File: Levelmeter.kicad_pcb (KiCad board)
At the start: 4 copper layers, 90 x 70 mm, 178 parts, among them J1 JST_PH_2.0mm_1x02, J10 Header_50mil_1x05, J11 Header_50mil_1x05, J2 USB_C, J3 Header_50mil_2x07, J4 JST_PH_2.0mm_1x03, J5 Header_100mil_1x06, J6 Header_100mil_1x06, J7 Header_100mil_1x06, J8 Header_50mil_1x03, J9 Header_50mil_1x05, Q1 DMG2305UX-13, Q2 DMG2305UX-13, Q3 FS8205A, Q4 AO3400A, Q5 AO3400A, SW1 PEC11R-4215F-S0024, SW2 PEC11R-4215F-S0024, U1 LP5907MFX-3.3/NOPB, U10 BL24C256A-SFRC, U11 BME280, U12 SN74HC14PWR, U13 LM35, U14 AD9833BRMZ-REEL7, U15 ADS131M04IPWR, U16 AD826, U2 DW01A, U3 LP5907MFX-3.3/NOPB, U4 TP4056, U5 HX4002-MFC, U6 LM27761DSGR, U7 STM32G0B1RET6, U8 RN4871-I/RM128, U9 SN74AHCT244DBR, Y1 Q13FC1350000400, Y2 X50328MSB2GI

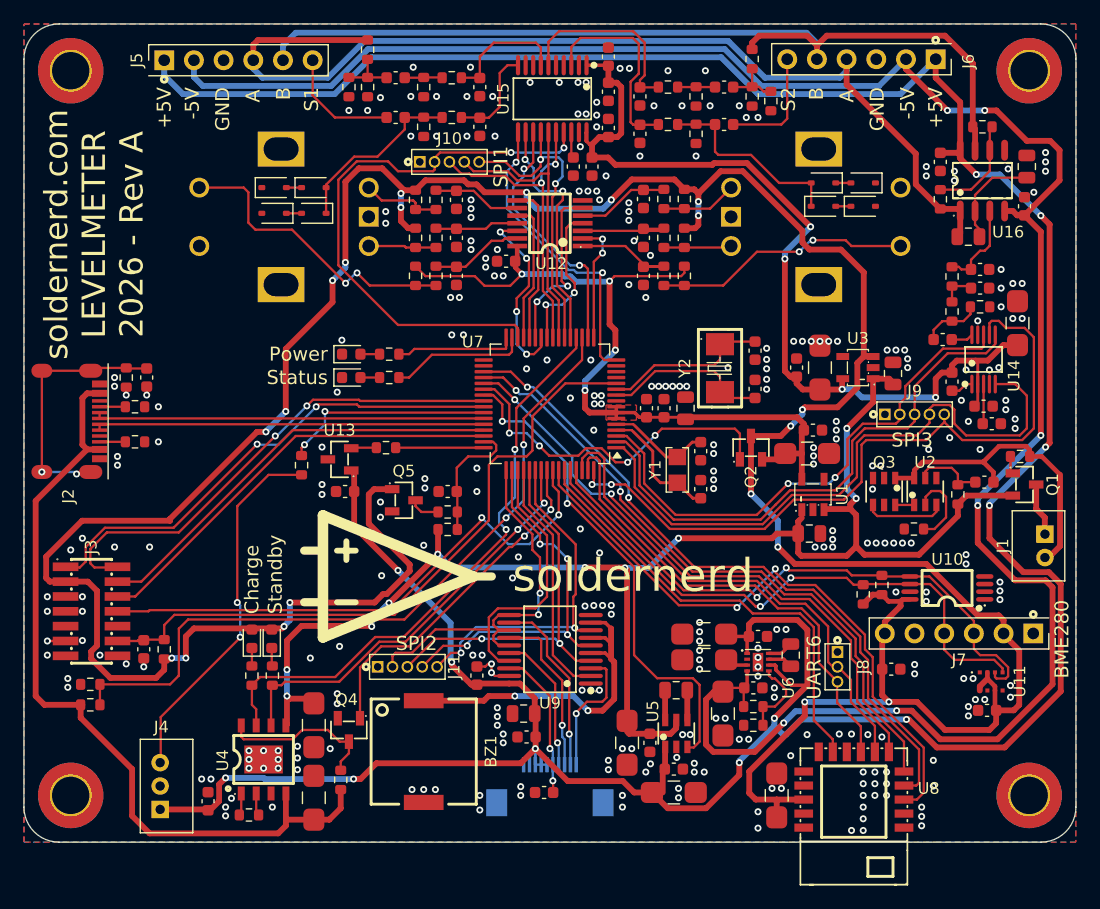
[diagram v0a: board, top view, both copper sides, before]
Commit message: Levelmeter sensor pinout changed. Font changed to bold
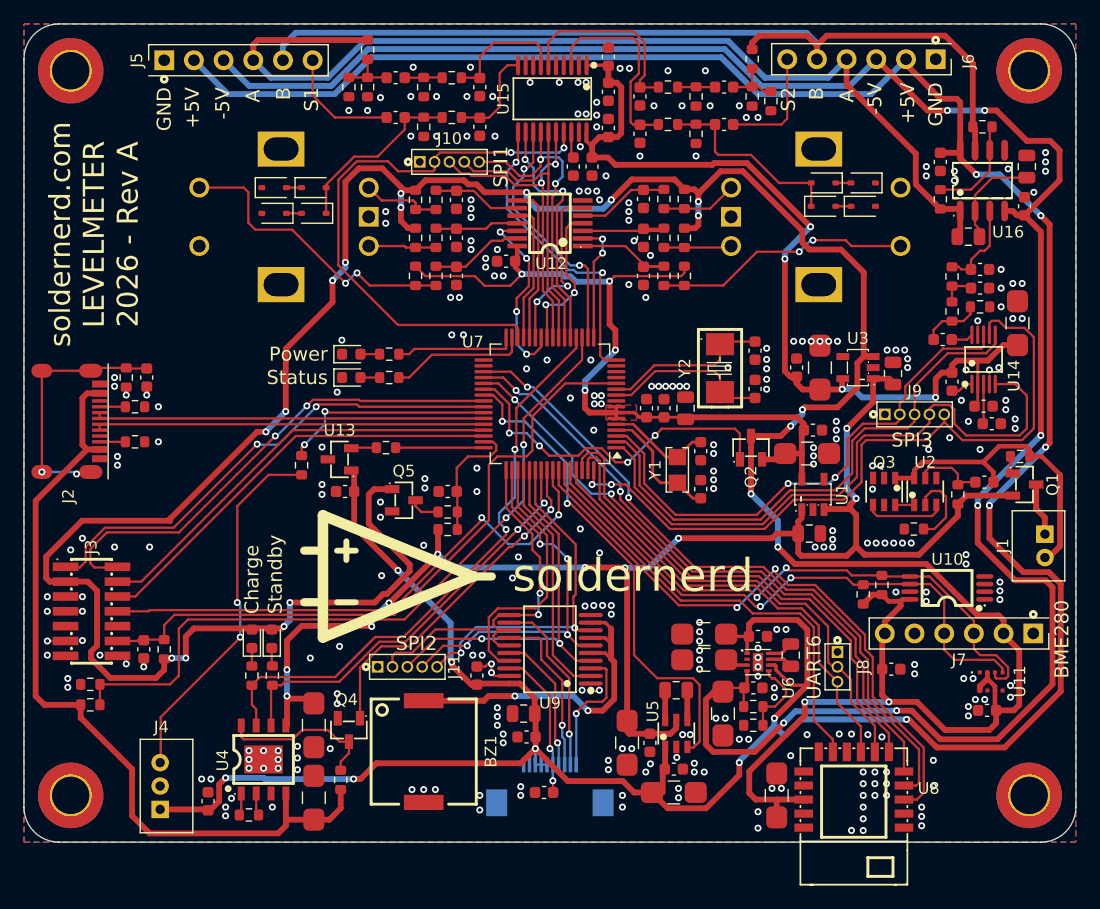
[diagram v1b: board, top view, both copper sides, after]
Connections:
- J5 pad 1: 5V0 -> GND
- J5 pad 2: -4V5 -> 5V0
- J5 pad 3: GND -> -4V5
- J6 pad 1: 5V0 -> GND
- J6 pad 2: -4V5 -> 5V0
- J6 pad 3: GND -> -4V5
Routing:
- net 5V0: track 292.1 -> 288.0 mm
- net -4V5: track 184.0 -> 180.0 mm
- net ExciterA: track 87.2 -> 86.0 mm

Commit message: Pinout description added, STM configuration added, netlist exported
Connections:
- net ~{CHARGE_EN} renamed CHARGE_EN
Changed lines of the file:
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@@
 			(size 1.25 0.7)
 			(layers "F.Cu" "F.Mask" "F.Paste")
-			(net "~{CHARGE_EN}")
+			(net "CHARGE_EN")
 			(pinfunction "G_1")
 			(pintype "unspecified")
@@
 			(layers "F.Cu" "F.Mask" "F.Paste")
 			(roundrect_rratio 0.25)
-			(net "~{CHARGE_EN}")
+			(net "CHARGE_EN")
 			(pinfunction "PD6_56")
 			(pintype "bidirectional")
@@
 	)
 	(segment
-		(start 94.75 68.175)
-		(end 94.75 70.375983)
-		(width 0.2)
-		(layer "F.Cu")
-		(net "~{CHARGE_EN}")
-	)
-	(segment
-		(start 94.75 70.375983)
-		(end 95.112744 70.738727)
-		(width 0.2)
-		(layer "F.Cu")
-		(net "~{CHARGE_EN}")
-	)
-	(segment
-		(start 91.75 74.75)
-		(end 91.5 74.75)
-		(width 0.2)
-		(layer "F.Cu")
-		(net "~{CHARGE_EN}")
-	)
-	(segment
-		(start 92.815687 73.815687)
-		(end 92.684313 73.815687)
-		(width 0.2)
-		(layer "F.Cu")
-		(net "~{CHARGE_EN}")
-	)
-	(segment
-		(start 92.684313 73.815687)
-		(end 91.75 74.75)
-		(width 0.2)
-		(layer "F.Cu")
-		(net "~{CHARGE_EN}")
-	)
-	(segment
-		(start 91.5 74.75)
-		(end 83 83.25)
-		(width 0.2)
-		(layer "F.Cu")
-		(net "~{CHARGE_EN}")
-	)
-	(segment
-		(start 83 83.25)
-		(end 80.565686 83.25)
-		(width 0.2)
-		(layer "F.Cu")
-		(net "~{CHARGE_EN}")
-	)
-	(segment
-		(start 95.112744 71.518631)
-		(end 95.078431 71.552944)
-		(width 0.2)
-		(layer "F.Cu")
-		(net "~{CHARGE_EN}")
-	)
-	(segment
-		(start 80.565686 83.25)
-		(end 78.75 85.065686)
-		(width 0.2)
-		(layer "F.Cu")
-		(net "~{CHARGE_EN}")
-	)
-	(segment
-		(start 78.75 85.065686)
-		(end 78.75 89.4)
-		(width 0.2)
-		(layer "F.Cu")
-		(net "~{CHARGE_EN}")
-	)
-	(segment
-		(start 95.112744 70.738727)
-		(end 95.112744 71.518631)
-		(width 0.2)
-		(layer "F.Cu")
-		(net "~{CHARGE_EN}")
-	)
-	(via
-		(at 92.815687 73.815687)
-		(size 0.6)
-		(drill 0.3)
-		(layers "F.Cu" "B.Cu")
-		(net "~{CHARGE_EN}")
-	)
-	(via
-		(at 95.078431 71.552944)
-		(size 0.6)
-		(drill 0.3)
-		(layers "F.Cu" "B.Cu")
-		(net "~{CHARGE_EN}")
-	)
-	(segment
-		(start 92.815687 73.815687)
-		(end 95.078431 71.552944)
-		(width 0.2)
-		(layer "B.Cu")
-		(net "~{CHARGE_EN}")
-	)
-	(segment
 		(start 119.45 45.6)
 		(end 120.75 45.6)
@@
 		(net "BAT+")
 	)
+	(segment
+		(start 94.75 68.175)
+		(end 94.75 70.375983)
+		(width 0.2)
+		(layer "F.Cu")
+		(net "CHARGE_EN")
+	)
+	(segment
+		(start 94.75 70.375983)
+		(end 95.112744 70.738727)
+		(width 0.2)
+		(layer "F.Cu")
+		(net "CHARGE_EN")
+	)
+	(segment
+		(start 91.75 74.75)
+		(end 91.5 74.75)
+		(width 0.2)
+		(layer "F.Cu")
+		(net "CHARGE_EN")
+	)
+	(segment
+		(start 92.815687 73.815687)
+		(end 92.684313 73.815687)
+		(width 0.2)
+		(layer "F.Cu")
+		(net "CHARGE_EN")
+	)
+	(segment
+		(start 92.684313 73.815687)
+		(end 91.75 74.75)
+		(width 0.2)
+		(layer "F.Cu")
+		(net "CHARGE_EN")
+	)
+	(segment
+		(start 91.5 74.75)
+		(end 83 83.25)
+		(width 0.2)
+		(layer "F.Cu")
+		(net "CHARGE_EN")
+	)
+	(segment
+		(start 83 83.25)
+		(end 80.565686 83.25)
+		(width 0.2)
+		(layer "F.Cu")
+		(net "CHARGE_EN")
+	)
+	(segment
+		(start 95.112744 71.518631)
+		(end 95.078431 71.552944)
+		(width 0.2)
+		(layer "F.Cu")
+		(net "CHARGE_EN")
+	)
+	(segment
+		(start 80.565686 83.25)
+		(end 78.75 85.065686)
+		(width 0.2)
+		(layer "F.Cu")
+		(net "CHARGE_EN")
+	)
+	(segment
+		(start 78.75 85.065686)
+		(end 78.75 89.4)
+		(width 0.2)
+		(layer "F.Cu")
+		(net "CHARGE_EN")
+	)
+	(segment
+		(start 95.112744 70.738727)
+		(end 95.112744 71.518631)
+		(width 0.2)
+		(layer "F.Cu")
+		(net "CHARGE_EN")
+	)
+	(via
+		(at 92.815687 73.815687)
+		(size 0.6)
+		(drill 0.3)
+		(layers "F.Cu" "B.Cu")
+		(net "CHARGE_EN")
+	)
+	(via
+		(at 95.078431 71.552944)
+		(size 0.6)
+		(drill 0.3)
+		(layers "F.Cu" "B.Cu")
+		(net "CHARGE_EN")
+	)
+	(segment
+		(start 92.815687 73.815687)
+		(end 95.078431 71.552944)
+		(width 0.2)
+		(layer "B.Cu")
+		(net "CHARGE_EN")
+	)
 	(zone

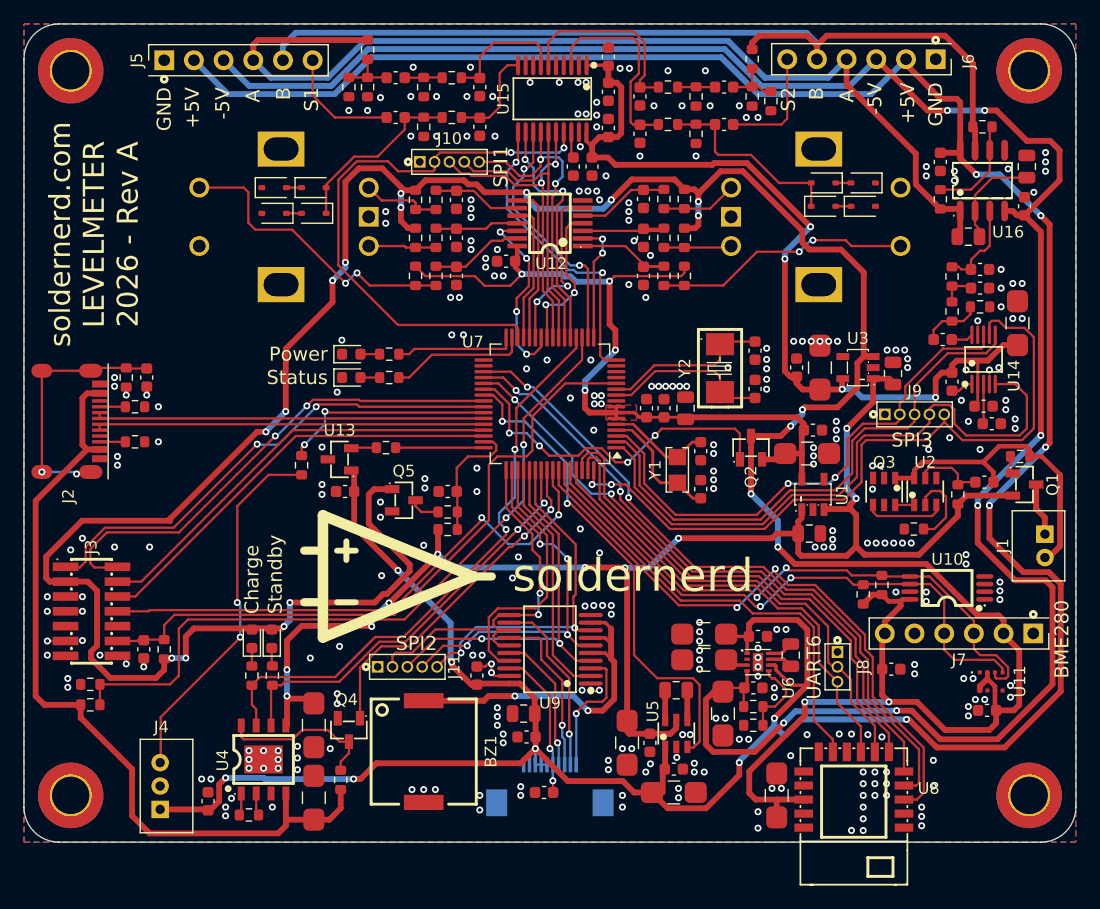
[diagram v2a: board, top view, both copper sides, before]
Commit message: Schematic checks, some smaller corrections, debug UART pinout corrected on programming header
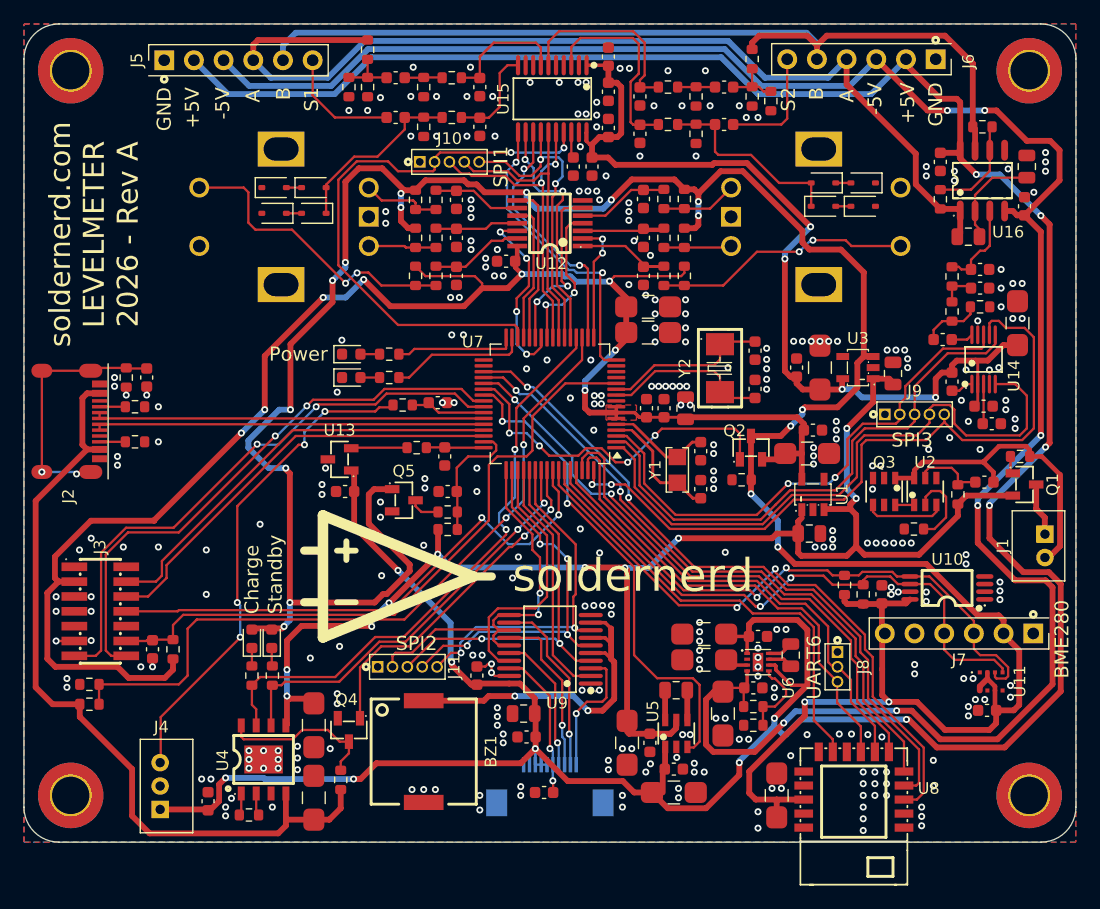
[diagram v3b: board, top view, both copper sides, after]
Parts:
- added C69: 10u, sldrnrd:C_1206, F.Cu at (103.4, 54.2)
- added C70: 10u, sldrnrd:C_1206, F.Cu at (103.4, 56.4)
- added C71: 1n, sldrnrd:C_0603, F.Cu at (85.4, 62.4)
- added C72: 1n, sldrnrd:C_0603, F.Cu at (86.0, 67.0)
- added R57: 100k, sldrnrd:R_0603, F.Cu at (111.4, 69.0)
- U13: value LM35 -> TMP236A4DBZR
- moved R35 10.1 mm to (82.4, 62.6), turned to 180 degrees
- moved C32 6.45 mm to (123.4, 78.8), turned to 90 degrees
- moved R20 3.20 mm to (120.2, 78.0)
- moved R28 2.62 mm to (83.6, 66.2)
- moved C45 0.75 mm to (61.0, 83.5)
- moved J3 0.75 mm to (56.5, 80.2)
- moved R34 0.75 mm to (62.8, 83.5)
- moved R32 0.09 mm to (55.6, 88.2)
- moved R33 0.07 mm to (55.6, 86.5)
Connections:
- net CHARGE_EN renamed ~{CHARGE_EN}
- J3 pad 01: DEBUG_UART_PC_TO_MCU -> unconnected-(J3-1-Pad01)
- J3 pad 02: DEBUG_UART_MCU_TO_PC -> unconnected-(J3-2-Pad02)
- J3 pad 03: 3V3 -> 3V3_STANDBY
- J3 pad 13: GND -> DEBUG_UART_PC_TO_MCU
- J3 pad 14: GND -> DEBUG_UART_MCU_TO_PC
- R34 pad 1: 3V3 -> 3V3_STANDBY
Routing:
- net 3V3_STANDBY: track 68.9 -> 144.0 mm, vias 4 -> 8
- net 3V3: track 284.8 -> 250.0 mm, vias 20 -> 18
- net TEMP_SENSE_EXT: track 18.2 -> 6.53 mm, vias 2 -> 0
- net Net-(J4-Pad3): track 31.5 -> 42.3 mm, vias 2 -> 4
- net DEBUG_UART_PC_TO_MCU: track 42.4 -> 49.7 mm
- net DEBUG_UART_MCU_TO_PC: track 42.7 -> 48.8 mm
- net Net-(U13-VOUT): track 2.01 -> 4.63 mm
- net TEMP_SENSE: track 7.53 -> 4.92 mm
- net EEPROM_SCL: track 49.7 -> 50.6 mm
- net ~{RST}: track 57.0 -> 56.3 mm
- net SWO: track 47.4 -> 46.7 mm
- net V_USB: track 69.5 -> 68.9 mm
- net GND: track 7.19 -> 7.26 mm, vias 316 -> 331
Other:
- board text removed: "Status"

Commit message: Further checks. Capacitors unified to basic parts
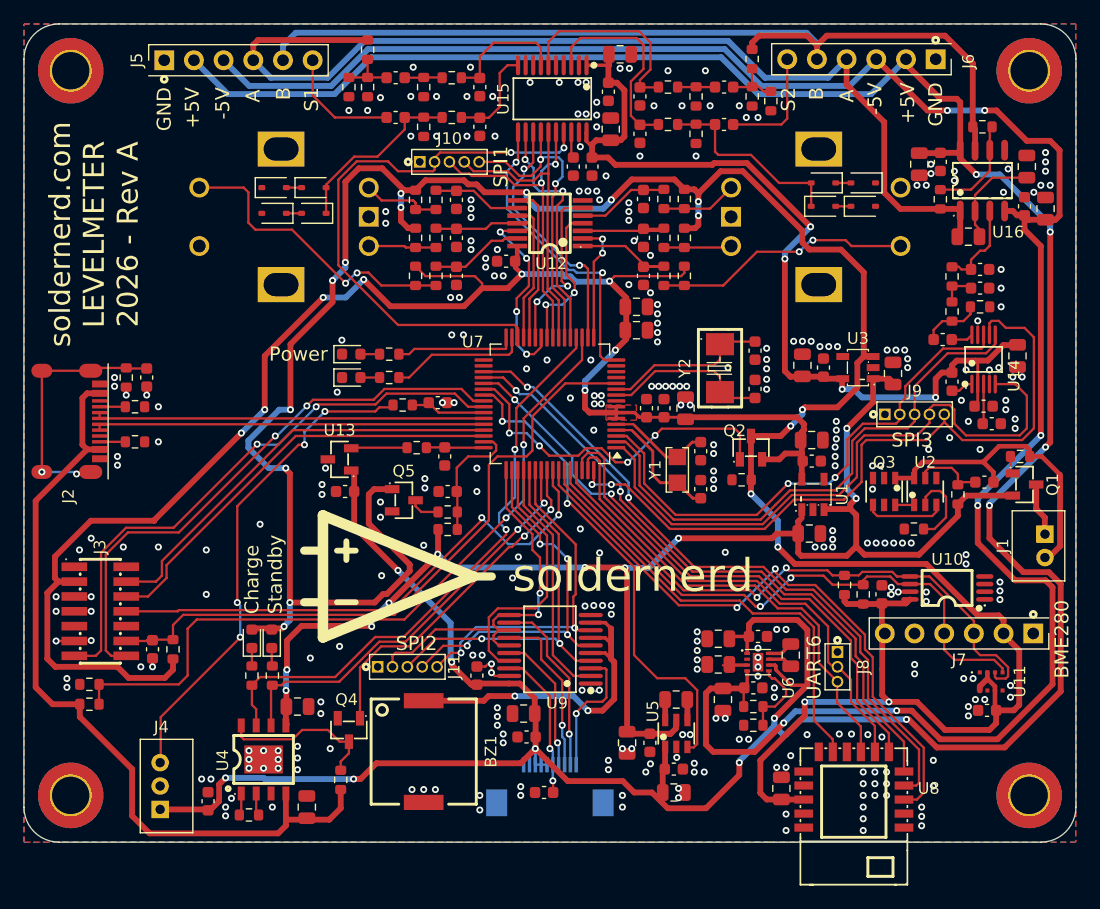
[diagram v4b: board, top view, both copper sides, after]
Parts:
- added C73: 10u, sldrnrd:C_0805, F.Cu at (137.4, 45.8)
- added C74: 10u, sldrnrd:C_0805, F.Cu at (126.6, 42.0)
- C11, C13, C16, C17, C20, C29, C3, C47, C69, C7, C70, C8, C9: footprint sldrnrd:C_1206 -> sldrnrd:C_0805
- C63, C64: footprint sldrnrd:C_0603 -> sldrnrd:C_0805
- moved C47 2.80 mm to (135.0, 58.4), turned to -90 degrees
- moved C2 2.65 mm to (117.4, 67.4)
- moved C6 2.30 mm to (118.4, 59.4)
- moved C11 2.13 mm to (73.4, 88.4), turned to 0 degrees
- moved C7 1.51 mm to (116.6, 59.2)
- moved C16 1.26 mm to (109.4, 84.8)
- moved C17 1.26 mm to (109.4, 82.6)
- moved C3 1.22 mm to (117.4, 65.6)
- moved C20 1.20 mm to (109.8, 87.8)
- moved C63 1.02 mm to (101.0, 32.6), turned to 0 degrees
- moved C70 1.02 mm to (102.4, 56.2)
- moved C69 1.00 mm to (102.4, 54.2)
- moved C9 1.00 mm to (74.2, 97.0)
- moved C14 0.80 mm to (105.8, 87.8)
- moved C29 0.72 mm to (114.8, 95.4)
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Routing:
- net -4V5: track 180.0 -> 182.8 mm
- net 3V3: track 250.0 -> 247.5 mm
- net ExciterA: track 86.0 -> 88.0 mm
- net 5V0: track 288.0 -> 289.8 mm
- net VCC: track 124.5 -> 123.2 mm
- net Net-(U5-C-): track 2.60 -> 1.75 mm
- net Net-(U5-C+): track 2.60 -> 1.75 mm
- net ExciterB_ADC: track 17.3 -> 18.0 mm
- net 5V_EN: track 42.1 -> 41.6 mm
- net GND: track 7.26 -> 7.19 mm, vias 331 -> 330

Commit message: LEVELMETER Rev A as ordered
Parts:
- added R58: 22R, sldrnrd:R_0603, F.Cu at (106.8, 72.6)
- added R59: 22R, sldrnrd:R_0603, F.Cu at (89.0, 55.8)
- BZ1: value CPT-9019A-SMT-TR -> CPT-9019S-SMT-TR; footprint sldrnrd:CPT-9019A -> sldrnrd:CPT-9019S
- C55, C56, C57, C58: value 1n -> 10n
- D2, D3: value LED_Green_0603 -> LED_Red_0603
- D4: value LED_Yellow_0603 -> LED_Red_0603
- Q1, Q2: value DMG2305UX-13 -> AO3401A
- R42, R43, R44, R45: value 33k -> 10k
- R46, R47, R48, R49: value 6k8 -> 680k
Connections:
- U7 pad 1: DAC_Clock -> Net-(U7-PC11)
- U7 pad 30: ADC_CLOCK -> Net-(U7-PB10)
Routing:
- net DAC_Clock: track 53.8 -> 42.7 mm
- net Net-(U7-PC11): track 0.00 -> 9.32 mm
- net ADC_CLOCK: track 48.8 -> 43.8 mm
- net Net-(U7-PB10): track 0.00 -> 3.36 mm
- net GND: vias 330 -> 337
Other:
- board text added: "I2C1"
- board text added: "UART3"
